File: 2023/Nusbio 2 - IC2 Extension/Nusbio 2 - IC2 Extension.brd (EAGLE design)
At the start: 44 x 50 mm, 9 parts

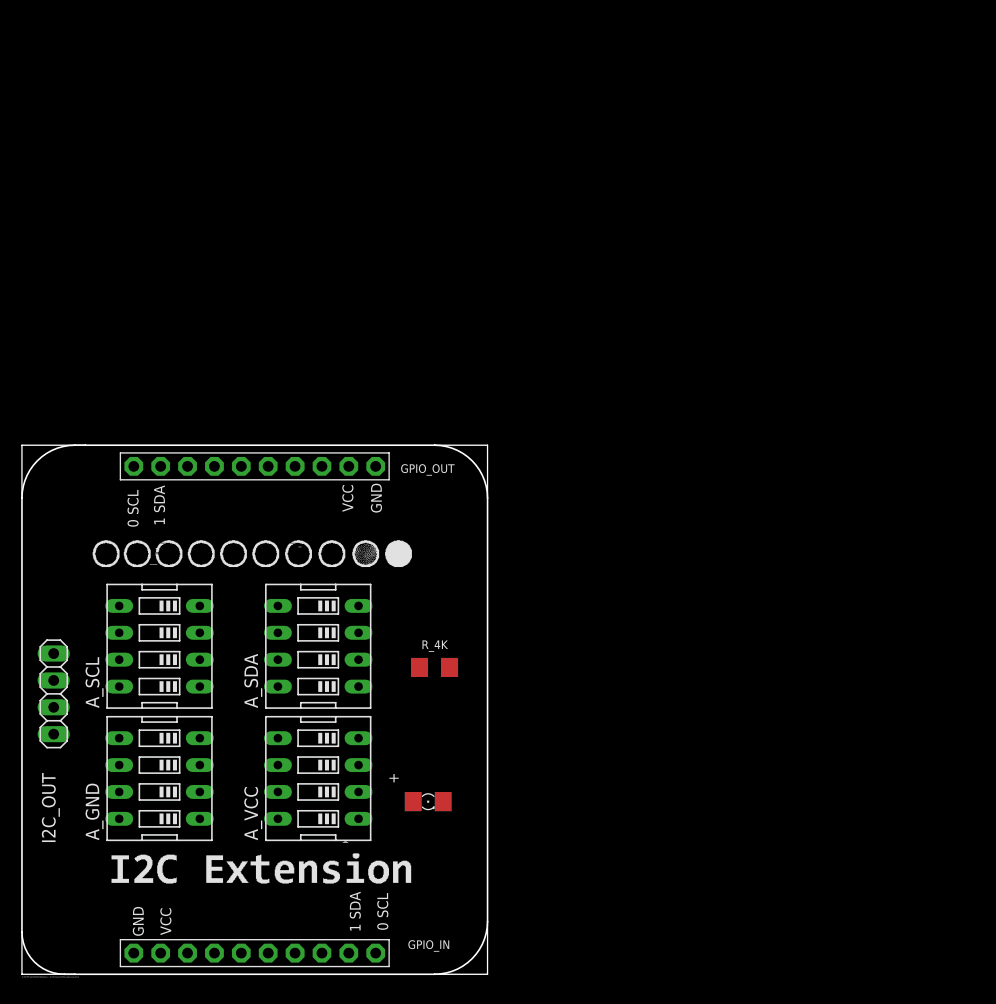
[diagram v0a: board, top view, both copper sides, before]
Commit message: Nusbio I2C Extension
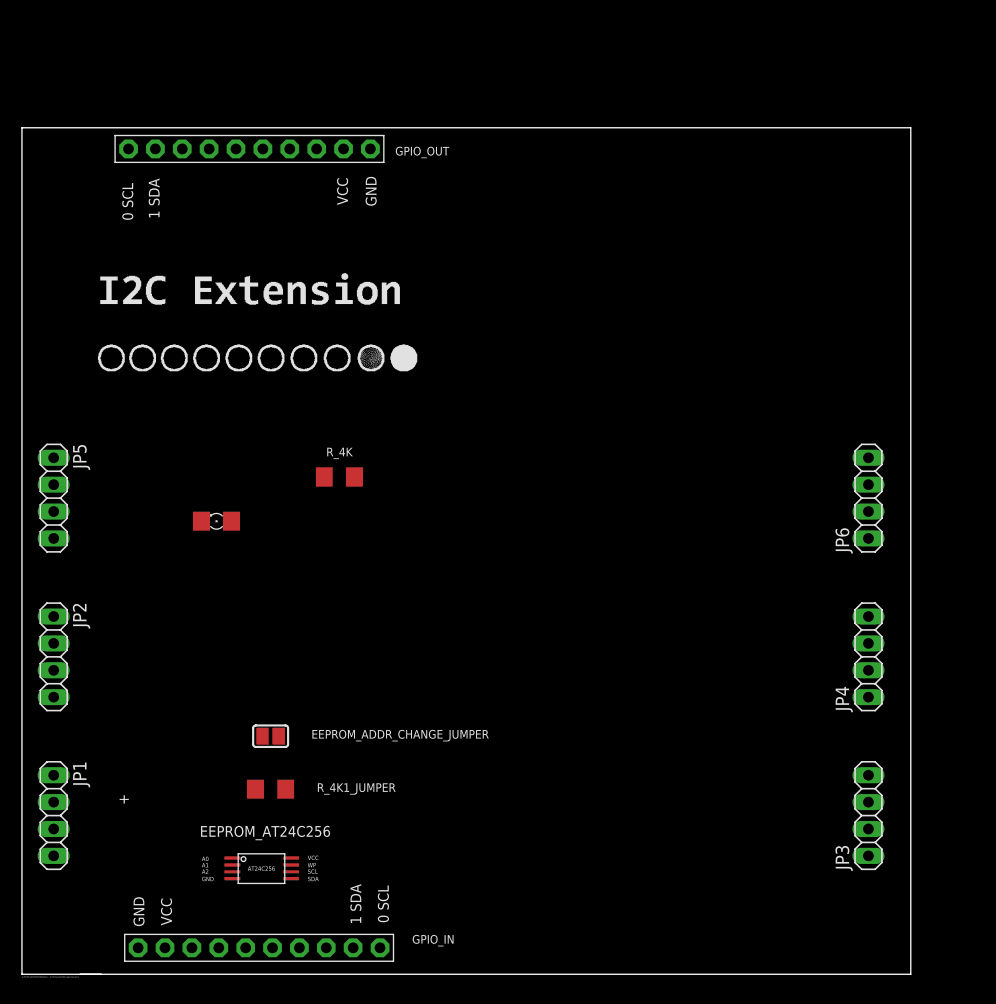
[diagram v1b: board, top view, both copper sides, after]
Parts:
- removed A_GND, A_SCL, A_SDA, A_VCC: (no value), special:EDG-04
- removed I2C_OUT: (no value), pinhead:1X04
- added EEPROM_ADDR_CHANGE_JUMPER: (no value), microbuilder:SOLDERJUMPER_REFLOW
- added EEPROM_AT24C256: DECADE-AT24C256-10TI-2.7, DECADE-libraries20151104:DECADE-AT24CXX
- added JP1, JP2, JP3, JP4, JP5, JP6: (no value), pinhead:1X04
- added R_4K1_JUMPER: (no value), adafruit:R1206
- moved LED_POWER 33.2 mm to (18.4, 42.8), turned to 180 degrees
- moved GPIO_OUT 30.0 mm to (21.5, 78.0)
- moved R_4K 20.1 mm to (30.0, 47.0), turned to 180 degrees
- moved GPIO_IN 0.65 mm to (22.4, 2.50)
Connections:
- removed net I2C_1: A_GND.1, A_SCL.1, A_SDA.1, A_VCC.1, I2C_OUT.1
- removed net I2C_2: A_GND.2, A_SCL.2, A_SDA.2, A_VCC.2, I2C_OUT.2
- removed net I2C_3: A_GND.3, A_SCL.3, A_SDA.3, A_VCC.3, I2C_OUT.3
- removed net I2C_4: A_GND.4, A_SCL.4, A_SDA.4, A_VCC.4, I2C_OUT.4
- new net N$1: EEPROM_AT24C256.VCC, EEPROM_AT24C256.WP
- new net N$6: EEPROM_ADDR_CHANGE_JUMPER.2, R_4K1_JUMPER.1
- net GND: now also EEPROM_ADDR_CHANGE_JUMPER.1, EEPROM_AT24C256.A0, EEPROM_AT24C256.A1, EEPROM_AT24C256.A2, EEPROM_AT24C256.GND, JP1.2, JP2.2, JP3.2, JP4.2, JP5.2, JP6.2; no longer A_GND.5, A_GND.6, A_GND.7, A_GND.8
- net SCL: now also EEPROM_AT24C256.SCL, JP1.3, JP2.3, JP3.3, JP4.3, JP5.3, JP6.3; no longer A_SCL.5, A_SCL.6, A_SCL.7, A_SCL.8
- net SDA: now also EEPROM_AT24C256.SDA, JP1.4, JP2.4, JP3.4, JP4.4, JP5.4, JP6.4; no longer A_SDA.5, A_SDA.6, A_SDA.7, A_SDA.8
- net VCC: now also JP1.1, JP2.1, JP3.1, JP4.1, JP5.1, JP6.1, R_4K1_JUMPER.2; no longer A_VCC.5, A_VCC.6, A_VCC.7, A_VCC.8
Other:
- board size 44 x 50 mm -> 84 x 80 mm
- board text added: "A0"
- board text added: "A1"
- board text added: "A2"
- board text added: "EEPROM_AT24C256"
- board text added: "SCL"
- board text added: "SDA"
- board text added: "WP"

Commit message: Nusbio I2C Extension
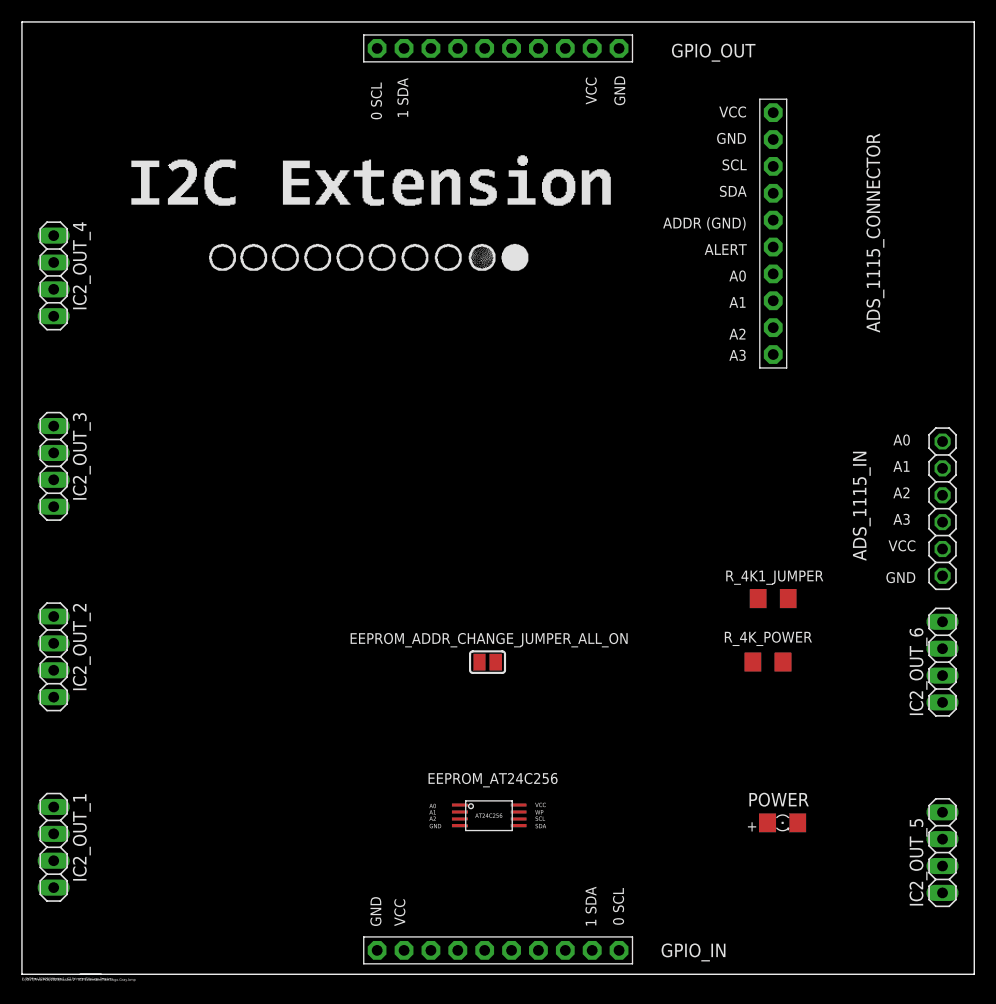
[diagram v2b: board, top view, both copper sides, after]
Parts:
- removed EEPROM_ADDR_CHANGE_JUMPER: (no value), microbuilder:SOLDERJUMPER_REFLOW
- removed JP1, JP3, JP4, JP5, JP6: (no value), pinhead:1X04
- removed R_4K: (no value), adafruit:R1206
- added ADS_1115_CONNECTOR: PINHD-1X10, adafruit:1X10-BIG
- added ADS_1115_IN: (no value), adafruit:1X06
- added EEPROM_ADDR_CHANGE_JUMPER_ALL_ON: (no value), microbuilder:SOLDERJUMPER_REFLOW
- added IC2_OUT_1, IC2_OUT_3, IC2_OUT_4, IC2_OUT_5, IC2_OUT_6: (no value), pinhead:1X04
- added R_4K_POWER: (no value), adafruit:R1206
- moved LED_POWER 60.6 mm to (71.9, 14.3), turned to 0 degrees
- moved R_4K1_JUMPER 50.8 mm to (71.0, 35.5)
- moved GPIO_OUT 25.3 mm to (45.0, 87.5)
- moved GPIO_IN 22.6 mm to (45.0, 2.26)
- moved EEPROM_AT24C256 22.1 mm to (44.1, 15.0)
- renumbered JP2 to IC2_OUT_2
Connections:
- new net ADS_A0: ADS_1115_CONNECTOR.7, ADS_1115_IN.6
- new net ADS_A1: ADS_1115_CONNECTOR.8, ADS_1115_IN.5
- new net ADS_A2: ADS_1115_CONNECTOR.9, ADS_1115_IN.4
- new net ADS_A3: ADS_1115_CONNECTOR.10, ADS_1115_IN.3
- new net ADS_ALERT: ADS_1115_CONNECTOR.6
- net GND: now also ADS_1115_CONNECTOR.2, ADS_1115_CONNECTOR.5, ADS_1115_IN.1, EEPROM_ADDR_CHANGE_JUMPER_ALL_ON.1, IC2_OUT_1.2, IC2_OUT_3.2, IC2_OUT_4.2, IC2_OUT_5.2, IC2_OUT_6.2, R_4K_POWER.1; no longer EEPROM_ADDR_CHANGE_JUMPER.1, JP1.2, JP3.2, JP4.2, JP5.2, JP6.2, R_4K.1
- net N$2: now also R_4K_POWER.2; no longer R_4K.2
- net N$6: now also EEPROM_ADDR_CHANGE_JUMPER_ALL_ON.2; no longer EEPROM_ADDR_CHANGE_JUMPER.2
- net SCL: now also ADS_1115_CONNECTOR.3, IC2_OUT_1.3, IC2_OUT_3.3, IC2_OUT_4.3, IC2_OUT_5.3, IC2_OUT_6.3; no longer JP1.3, JP3.3, JP4.3, JP5.3, JP6.3
- net SDA: now also ADS_1115_CONNECTOR.4, IC2_OUT_1.4, IC2_OUT_3.4, IC2_OUT_4.4, IC2_OUT_5.4, IC2_OUT_6.4; no longer JP1.4, JP3.4, JP4.4, JP5.4, JP6.4
- net VCC: now also ADS_1115_CONNECTOR.1, ADS_1115_IN.2, IC2_OUT_1.1, IC2_OUT_3.1, IC2_OUT_4.1, IC2_OUT_5.1, IC2_OUT_6.1; no longer JP1.1, JP3.1, JP4.1, JP5.1, JP6.1
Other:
- board size 84 x 80 mm -> 90 x 90 mm
- board text added: "A3"
- board text added: "ADDR (GND)"
- board text added: "ALERT"
- board text added: "POWER"

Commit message: Nusbio test extension
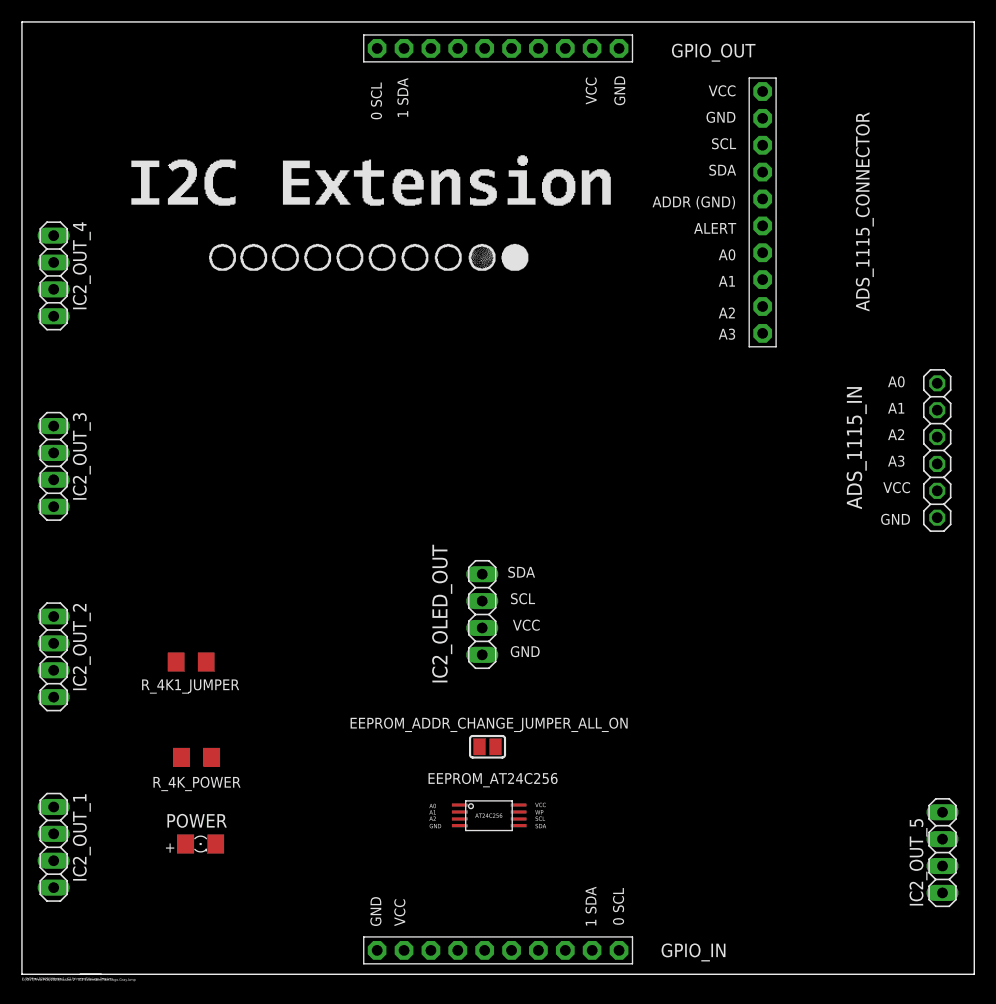
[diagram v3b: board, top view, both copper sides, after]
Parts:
- removed IC2_OUT_6: (no value), pinhead:1X04
- added IC2_OLED_OUT: (no value), pinhead:1X04
- moved R_4K1_JUMPER 55.3 mm to (16.0, 29.5), turned to 180 degrees
- moved LED_POWER 55.0 mm to (16.9, 12.3)
- moved R_4K_POWER 54.7 mm to (16.5, 20.5), turned to 0 degrees
- moved EEPROM_ADDR_CHANGE_JUMPER_ALL_ON 8.00 mm to (44.0, 21.5)
- moved ADS_1115_IN 5.52 mm to (86.5, 49.5)
- moved ADS_1115_CONNECTOR 2.24 mm to (70.0, 72.0)
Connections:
- net GND: now also IC2_OLED_OUT.1; no longer IC2_OUT_6.2
- net SCL: now also IC2_OLED_OUT.3; no longer IC2_OUT_6.3
- net SDA: now also IC2_OLED_OUT.4; no longer IC2_OUT_6.4
- net VCC: now also IC2_OLED_OUT.2; no longer IC2_OUT_6.1

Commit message: Nusbio v2 pcb and SPIExtension v 1 2023/05
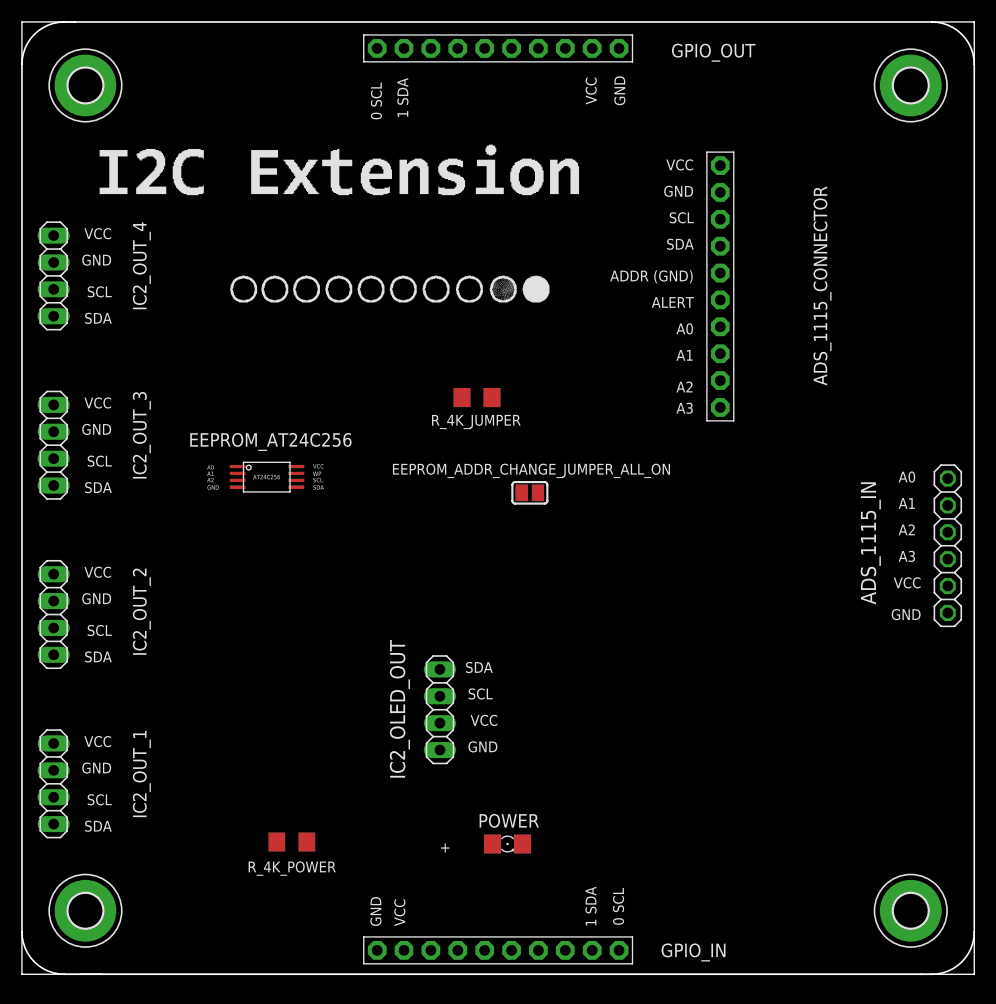
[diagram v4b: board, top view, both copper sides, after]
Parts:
- removed IC2_OUT_5: (no value), pinhead:1X04
- removed R_4K1_JUMPER: (no value), adafruit:R1206
- added H1, H2, H3, H4: MOUNT-PAD-ROUND3.3, holes:3,3-PAD
- added R_4K_JUMPER: (no value), adafruit:R1206
- moved EEPROM_AT24C256 38.3 mm to (23.1, 47.0)
- moved LED_POWER 29.0 mm to (45.9, 12.3)
- moved EEPROM_ADDR_CHANGE_JUMPER_ALL_ON 24.3 mm to (48.0, 45.5)
- moved R_4K_POWER 12.0 mm to (25.5, 12.5)
- moved IC2_OLED_OUT 9.85 mm to (39.5, 25.0)
- moved ADS_1115_IN 9.06 mm to (87.5, 40.5)
- moved ADS_1115_CONNECTOR 8.06 mm to (66.0, 65.0)
- moved IC2_OUT_1 6.00 mm to (3.00, 18.0)
- moved IC2_OUT_2 4.00 mm to (3.00, 34.0)
- moved IC2_OUT_3 2.00 mm to (3.00, 50.0)
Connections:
- net GND: now also EEPROM_AT24C256.WP; no longer IC2_OUT_5.2
- net N$1: no longer EEPROM_AT24C256.WP
- net N$6: now also R_4K_JUMPER.1; no longer R_4K1_JUMPER.1
- net SCL: no longer IC2_OUT_5.3
- net SDA: no longer IC2_OUT_5.4
- net VCC: now also R_4K_JUMPER.2; no longer IC2_OUT_5.1, R_4K1_JUMPER.2
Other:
- outline, holes or cut-outs redrawn
- board text added: "PCBv1 - 2023.05"
- board text removed: "C:/DVT/Fred.PCB/2023/Nusbio 2 - IC2 Extension/Title.Logo.Gray.bmp"
- board text removed: "PCBv2 - 2023.03"

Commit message: Nusbio v2 pcb and SPIExtension v 1 2023/05
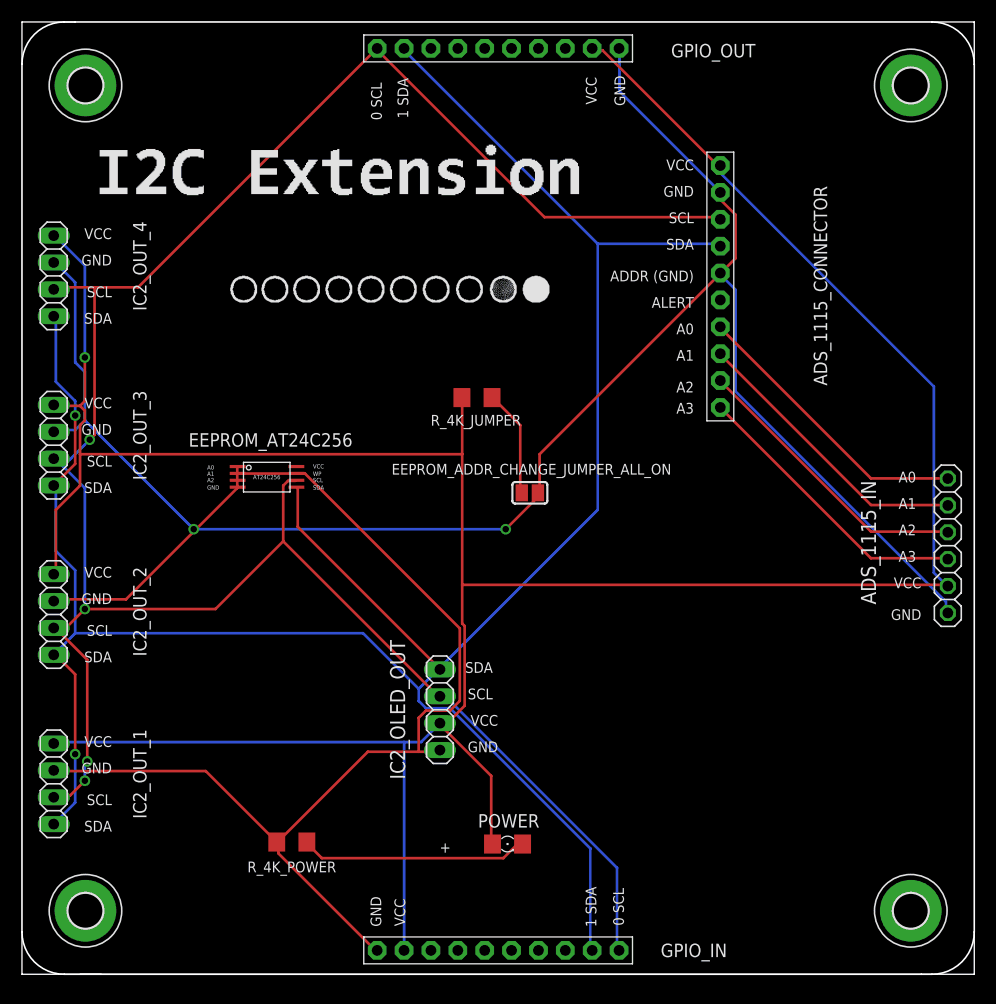
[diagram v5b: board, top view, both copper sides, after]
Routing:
- net VCC: track 0.00 -> 288.0 mm, vias 0 -> 1
- net GND: track 0.00 -> 286.7 mm, vias 0 -> 2
- net SDA: track 0.00 -> 230.7 mm, vias 0 -> 2
- net SCL: track 0.00 -> 218.1 mm, vias 0 -> 4
- net ADS_A0: track 0.00 -> 27.5 mm
- net ADS_A1: track 0.00 -> 27.5 mm
- net ADS_A2: track 0.00 -> 27.4 mm
- net ADS_A3: track 0.00 -> 27.4 mm
- net N$2: track 0.00 -> 21.6 mm
- net N$6: track 0.00 -> 10.2 mm

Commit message: Fix Nusbio I2Cextension with right eeprom format
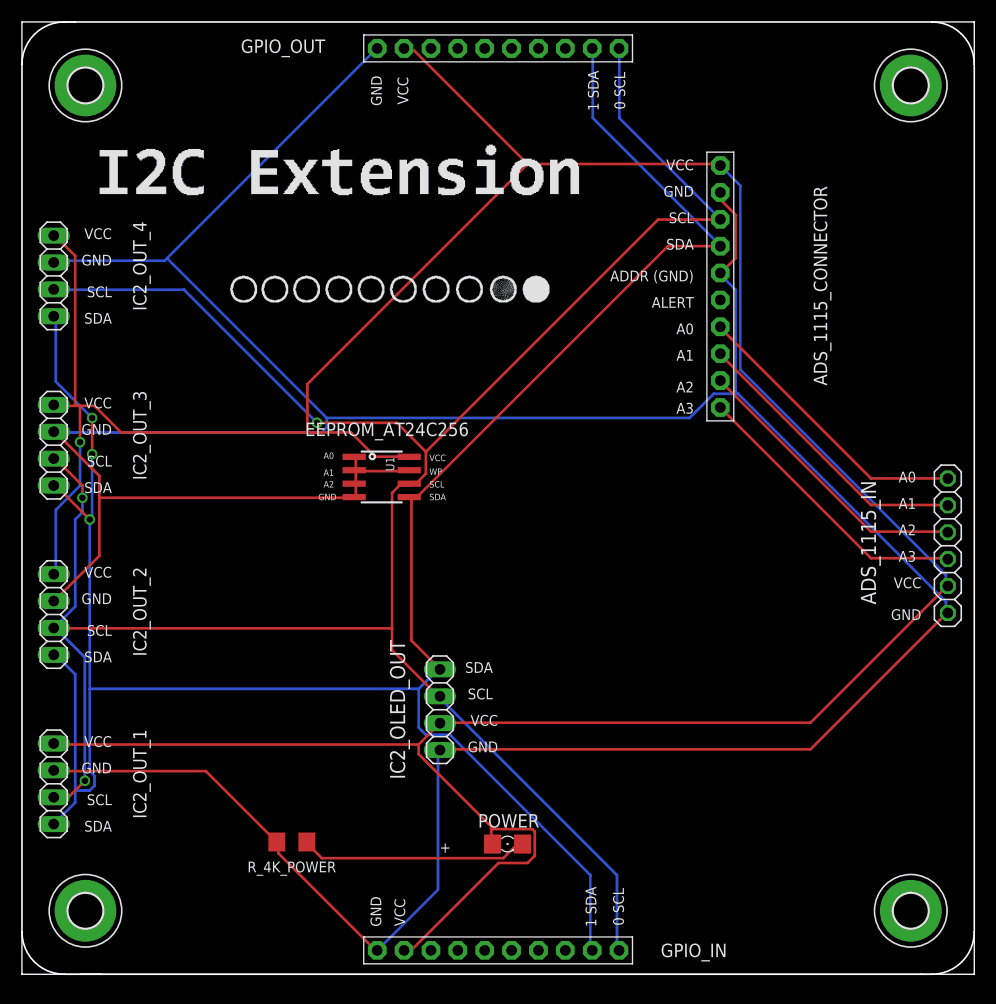
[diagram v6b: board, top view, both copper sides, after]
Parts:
- removed EEPROM_ADDR_CHANGE_JUMPER_ALL_ON: (no value), microbuilder:SOLDERJUMPER_REFLOW
- removed EEPROM_AT24C256: DECADE-AT24C256-10TI-2.7, DECADE-libraries20151104:DECADE-AT24CXX
- removed R_4K_JUMPER: (no value), adafruit:R1206
- added U1: (no value), microbuilder:SOIC8_150MIL
- turned GPIO_OUT to 180 degrees
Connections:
- removed net N$1: EEPROM_AT24C256.VCC
- removed net N$6: EEPROM_ADDR_CHANGE_JUMPER_ALL_ON.2, R_4K_JUMPER.1
- net GND: now also U1.1, U1.2, U1.3, U1.4, U1.7; no longer EEPROM_ADDR_CHANGE_JUMPER_ALL_ON.1, EEPROM_AT24C256.A0, EEPROM_AT24C256.A1, EEPROM_AT24C256.A2, EEPROM_AT24C256.GND, EEPROM_AT24C256.WP
- net SCL: now also U1.6; no longer EEPROM_AT24C256.SCL
- net SDA: now also U1.5; no longer EEPROM_AT24C256.SDA
- net VCC: now also U1.8; no longer R_4K_JUMPER.2
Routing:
- net GND: track 286.7 -> 342.8 mm, vias 2 -> 0
- net VCC: track 288.0 -> 312.4 mm
- net SDA: track 230.7 -> 218.0 mm, vias 2 -> 3
- net N$6: track 10.2 -> 0.00 mm
- net SCL: track 218.1 -> 226.5 mm, vias 4 -> 3
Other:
- board text added: "PCBv2 - 2023.10"
- board text removed: "PCBv1 - 2023.05"
